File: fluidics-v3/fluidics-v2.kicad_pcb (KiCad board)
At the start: 4 copper layers, 82.5 x 95.5 mm, 77 parts, among them IC2 ADUM1250WSRZ-RL7, J1 PJ-063AH, J10 87832-1010, J11 0705430001, J12 87832-1010, J13 0705430001, J14 87832-1010, J15 0533980671, J16 0705430001, J17 0533980671, J18 87832-1010, J19 0705430001, J2 B6B-ZR-SM4-TF, J20 0533980671, J21 87832-1010, J22 0705430001, J24 0705430001, J25 87832-1010, J3 A-DS_15_A_KG-T4S, J4 B6B-ZR-SM4-TF, J5 Screw_Terminal_01x02, J6 Screw_Terminal_01x02, U1 TPL7407LDR, U11 MAX3221, U12 CD4050BDR, U13 TC7PZ17FU, U2 Teensy4.1, U3 AP7366EA-33W5-7, U4 D24V10FX, U6 LTC4311CSC6-TRPBF

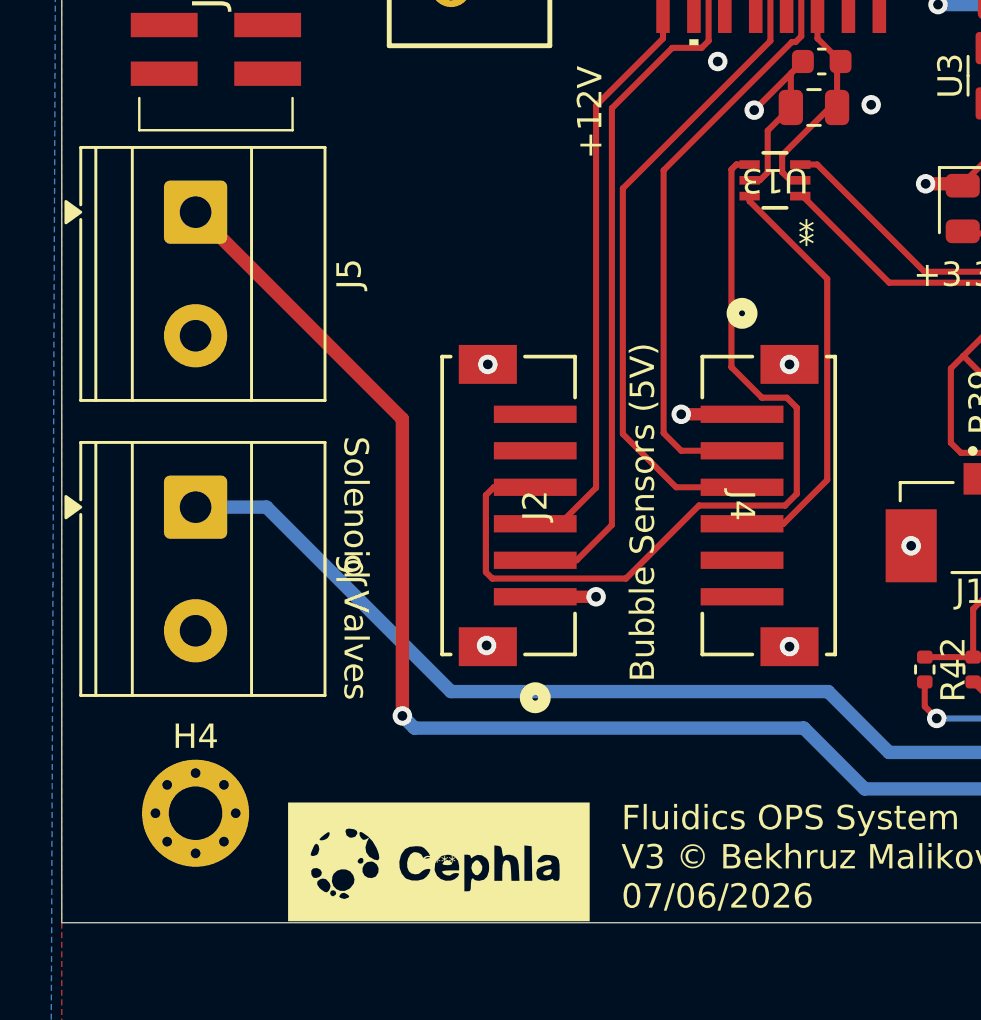
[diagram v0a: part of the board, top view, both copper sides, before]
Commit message: Swap 2x terminal blocks MKDS-1,5-2-5.08 -> MPT-0,5-2-2.54
Replace two 1x02 Phoenix terminal blocks with the smaller MPT series
(2.54mm pitch, 5.54x6.20mm body vs 10.16x9.80mm) to reclaim board space.
Schematic + PCB updated; DRC parity 0. Note: MPT rated for 0.5mm2 wire
(vs 1.5mm2 on MKDS) - lower current/wire-gauge capacity.

Co-Authored-By: Claude Opus 4.8 (1M context) <noreply@anthropic.com>
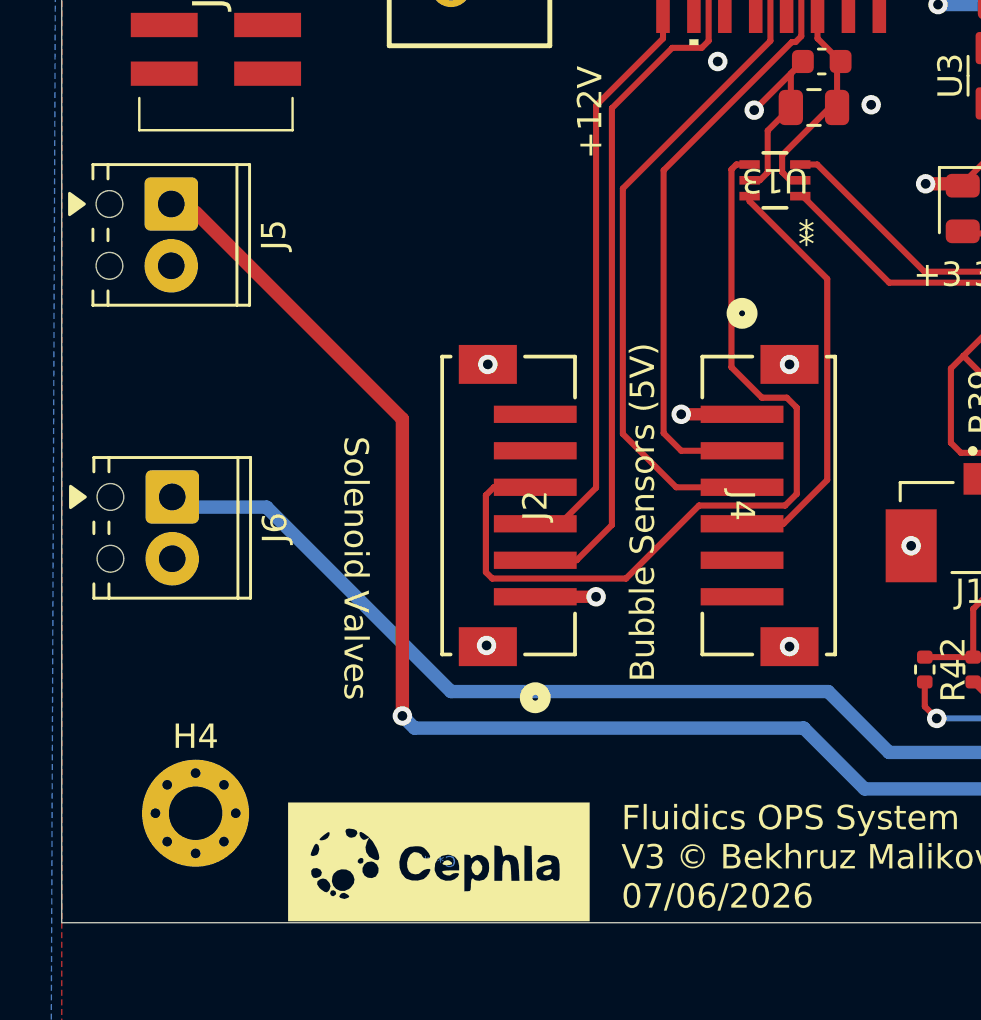
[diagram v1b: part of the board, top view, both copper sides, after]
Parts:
- J5, J6: footprint TerminalBlock_Phoenix:TerminalBlock_Phoenix_MKDS-1,5-2-5.08_1x02_P5.08mm_Horizontal -> TerminalBlock_Phoenix:TerminalBlock_Phoenix_MPT-0,5-2-2.54_1x02_P2.54mm_Horizontal
- moved J5 1.05 mm to (114.0, 87.0)
- moved J6 1.05 mm to (114.0, 99.0)
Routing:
- net Net-(J5-Pin_1): track 109.2 -> 110.4 mm
- net Net-(J6-Pin_1): track 91.1 -> 92.3 mm

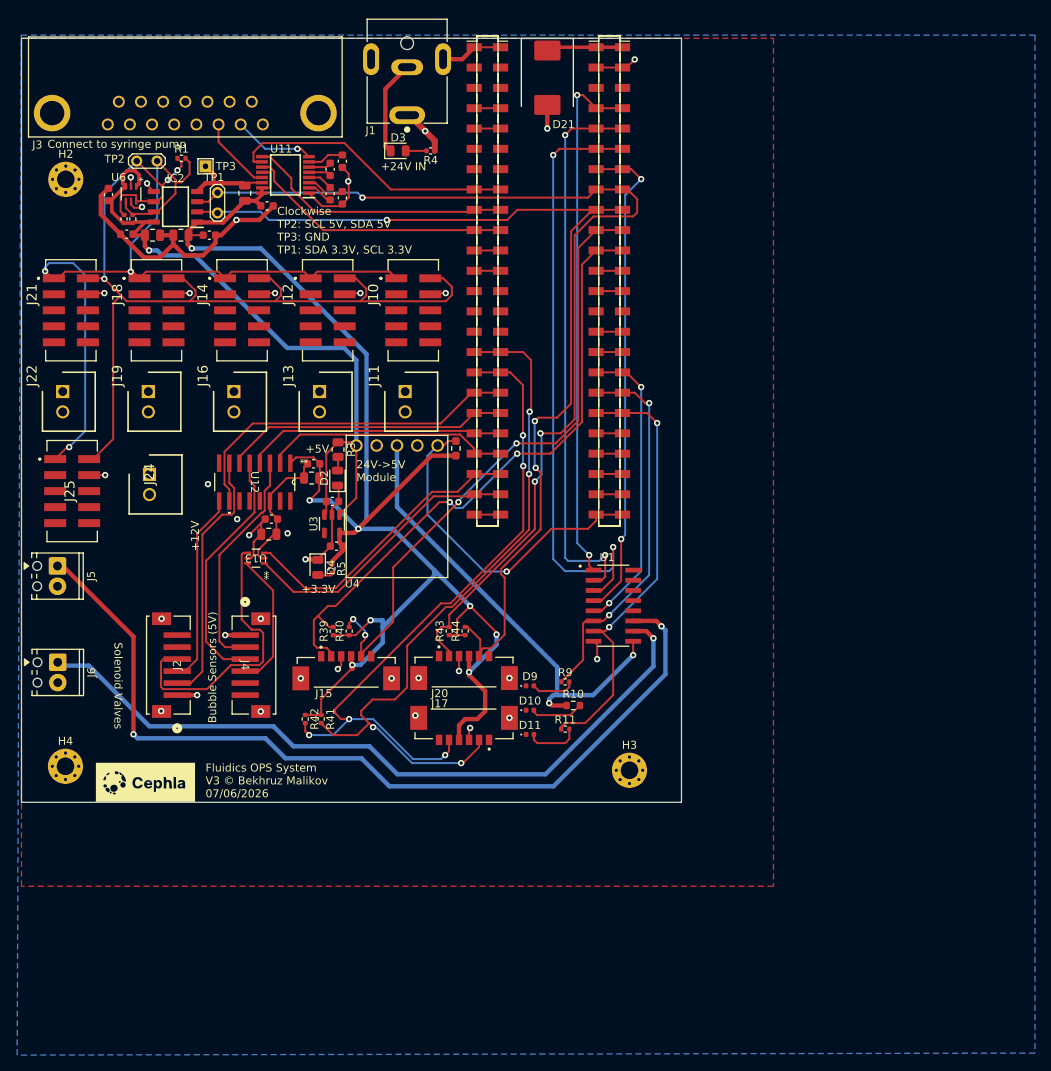
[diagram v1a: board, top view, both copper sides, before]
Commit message: Add GPIO_5 status LED and +24V screw terminal J7
- Root sheet: GPIO_5 status LED (D12 + R12 2.7K to GND)
- Solenoid driver sheet: J7 2-pin screw terminal (pin2 = +24V)

Schematic parses clean via kicad-cli; D12/R12/J7 present in netlist.

Co-Authored-By: Claude Opus 4.8 (1M context) <noreply@anthropic.com>
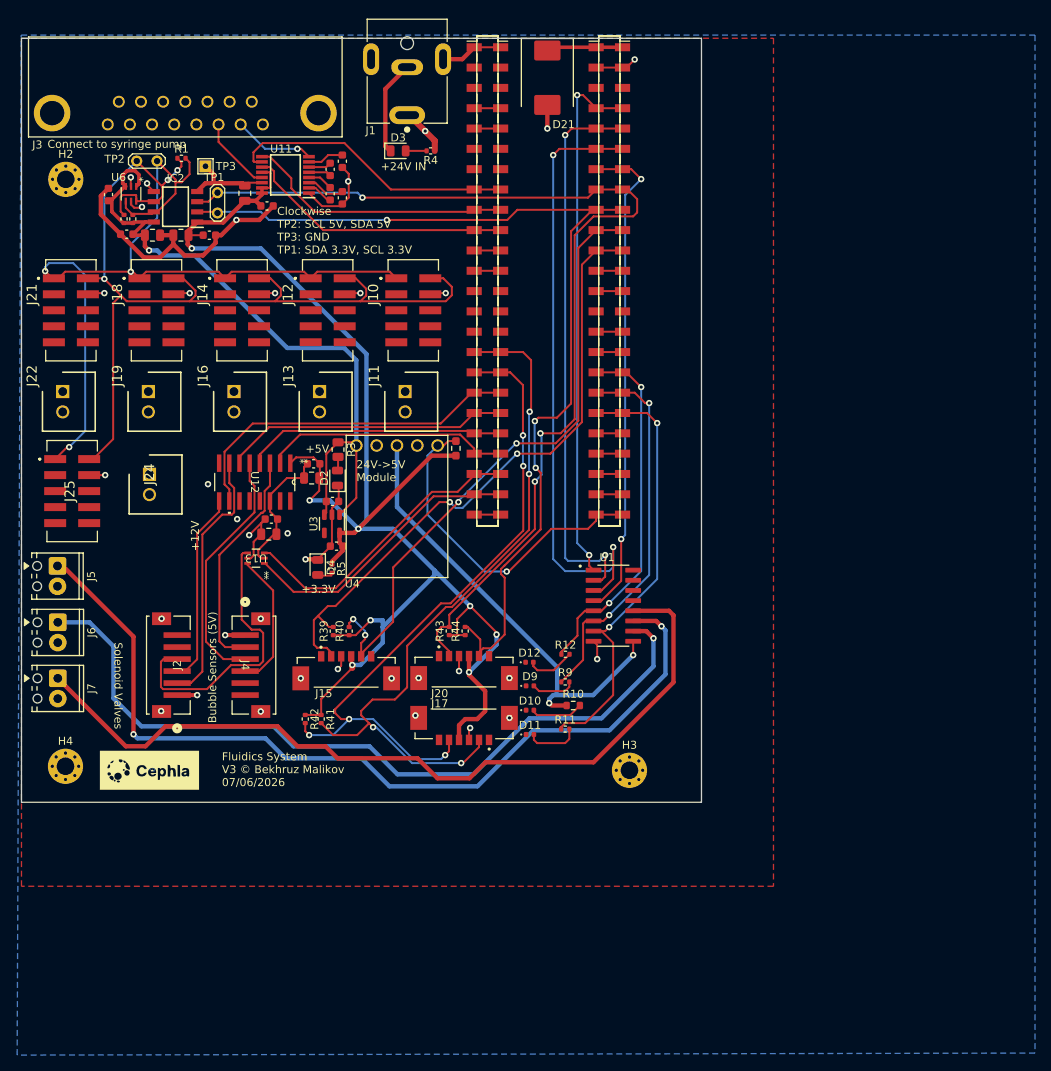
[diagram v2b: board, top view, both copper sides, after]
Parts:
- added D12: LED, LED_SMD:LED_0402_1005Metric, F.Cu at (173.0, 99.0)
- added J7: Screw_Terminal_01x02, TerminalBlock_Phoenix:TerminalBlock_Phoenix_MPT-0,5-2-2.54_1x02_P2.54mm_Horizontal, F.Cu at (114.0, 101.0)
- added R12: 2.7K, Resistor_SMD:R_0402_1005Metric, F.Cu at (177.5, 98.0)
- moved J6 5.00 mm to (114.0, 94.0)
- moved G*** 1.58 mm to (125.5, 112.5)
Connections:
- U1 pad 12: unconnected-(U1-OUT5-Pad12) -> Net-(J7-Pin_1)
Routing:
- net Net-(J7-Pin_1): track 0.00 -> 102.8 mm
- net /GPIO_5: track 37.4 -> 45.1 mm
- net Net-(D12-A): track 0.00 -> 6.05 mm
- net Net-(J6-Pin_1): track 92.3 -> 98.1 mm
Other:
- board size 82.5 x 95.5 mm -> 85 x 95.5 mm
- board text added: "Fluidics System V3 © Bekhruz Malikov 07/06/2026"
- board text removed: "Fluidics OPS System V3 © Bekhruz Malikov 07/06/2026"

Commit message: Consolidate solenoid outputs to single 1x06 terminal J5
Replace 3x 1x02 blocks (J5/J6/J7) with one 6-position Xinya XY308-2.54-6P
(J5): pads 1/3/5 = U1 TPL7407 OUT5/6/7, pads 2/4/6 = +24V. DRC electrically
clean (0 clearance/shorting; 5 unconnected are intentional U2 GPIO/SPI NC).

Assign 3D model: KiCad 10 ships no Xinya XY308 .step, so point J5's model at
the bundled Phoenix MPT-0,5-6-2.54 1x06 (same pitch/positions) for the 3D
preview. Footprint/BOM/CPL still reference the real Xinya part.

Co-Authored-By: Claude Opus 4.8 (1M context) <noreply@anthropic.com>
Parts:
- removed J6, J7: Screw_Terminal_01x02, TerminalBlock_Phoenix:TerminalBlock_Phoenix_MPT-0,5-2-2.54_1x02_P2.54mm_Horizontal
- J5: value Screw_Terminal_01x02 -> Screw_Terminal_01x06; footprint TerminalBlock_Phoenix:TerminalBlock_Phoenix_MPT-0,5-2-2.54_1x02_P2.54mm_Horizontal -> TerminalBlock:TerminalBlock_Xinya_XY308-2.54-6P_1x06_P2.54mm_Horizontal
- moved J5 3.61 mm to (116.0, 90.0)
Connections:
- U1 pad 10: Net-(J6-Pin_1) -> Net-(J5-Pin_5)
- U1 pad 11: Net-(J5-Pin_1) -> Net-(J5-Pin_3)
- U1 pad 12: Net-(J7-Pin_1) -> Net-(J5-Pin_1)
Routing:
- net Net-(J7-Pin_1): track 102.8 -> 0.00 mm
- net Net-(J5-Pin_3): track 0.00 -> 101.1 mm, vias 0 -> 2
- net Net-(J6-Pin_1): track 98.1 -> 0.00 mm, vias 1 -> 0
- net Net-(J5-Pin_5): track 0.00 -> 89.8 mm, vias 0 -> 1
- net Net-(J5-Pin_1): track 110.4 -> 123.3 mm, vias 2 -> 1

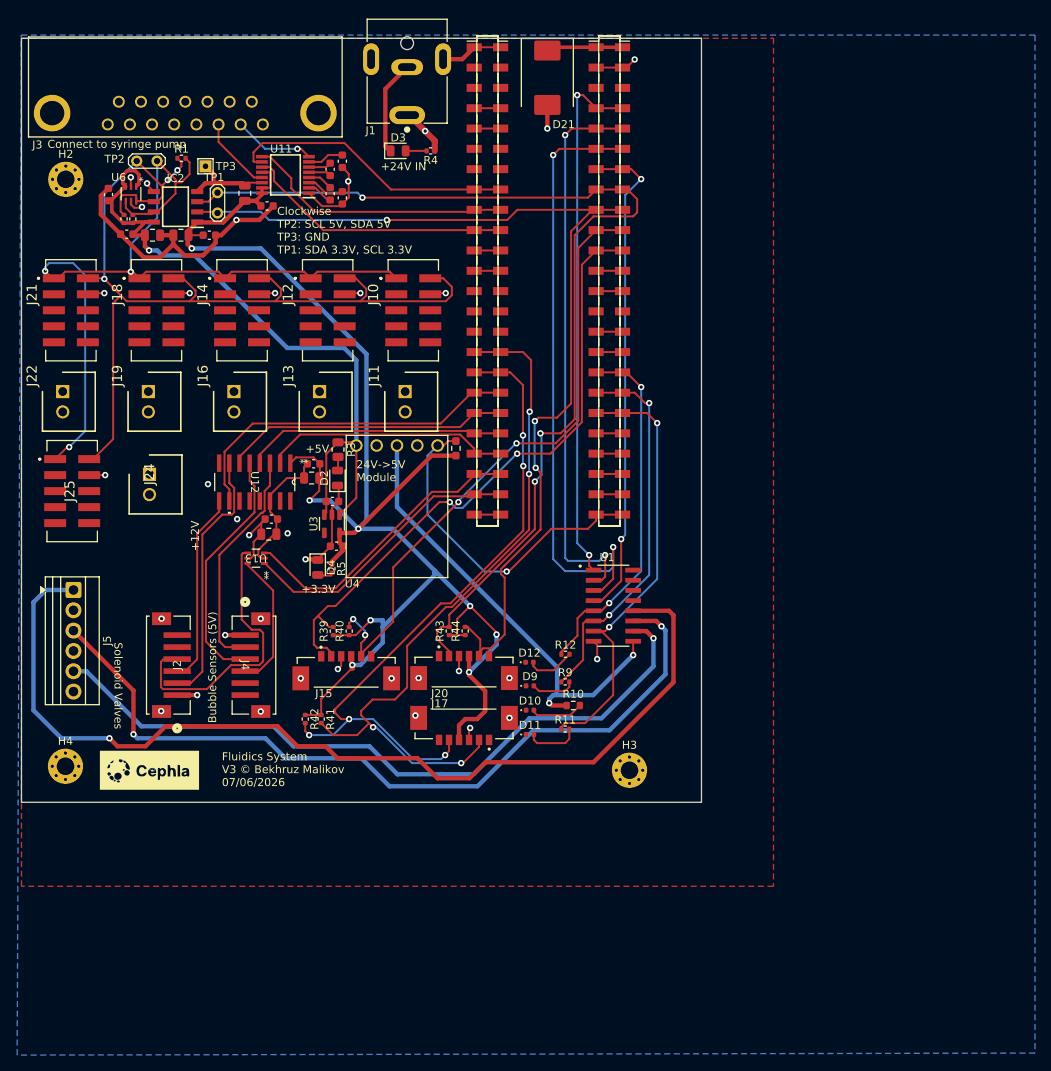
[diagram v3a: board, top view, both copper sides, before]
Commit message: v3 PCB: 3.3V power-plane islands + B.Cu bridge, refdes to F.Fab, block silk labels
PCB (this session, verified DRC-clean, 0 electrical regressions):
- Add +3.3V copper islands on In2.Cu (top U11/IC2 cluster + LDO/I2C-connector corner)
- Add +3.3V bridge pour on B.Cu down the inter-island corridor; delete ~18mm redundant vertical run
- Stitch 3.3V loads to islands with vias; remove ~35mm circuitous surface routing (3.3V trace 194->68mm)
- Move 21 hidden reference designators (caps, R22/R23/R51, U2 Teensy) to F.Fab, centered
- Add functional F.Silkscreen labels: Solenoid Driver, Flow, I2C Iso, RS-232

Also bundles accompanying schematic/library work not authored this session
(fluidics-v2.kicad_sch, svalves, solenoid_driver, 87832-0410 Molex connector lib).

Co-Authored-By: Claude Opus 4.8 (1M context) <noreply@anthropic.com>
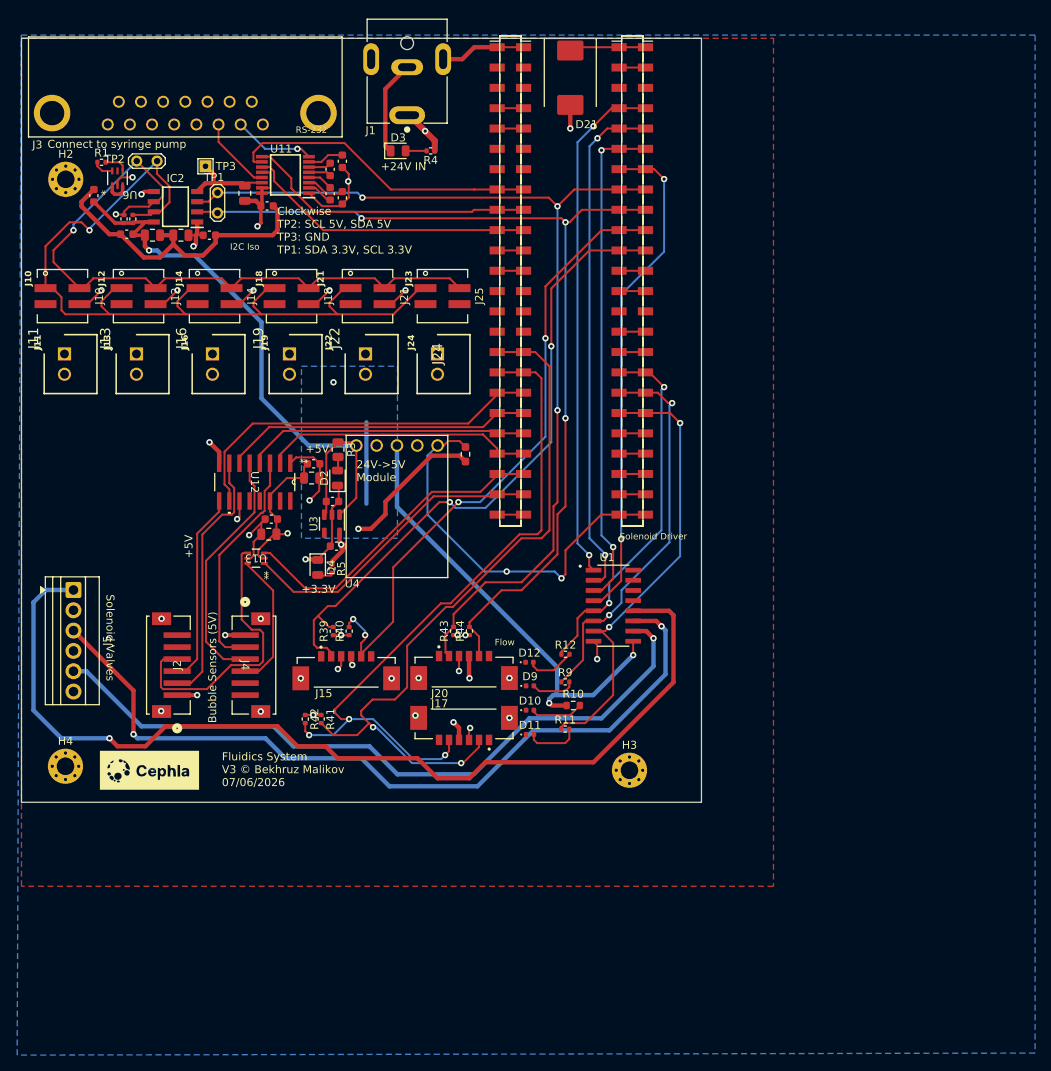
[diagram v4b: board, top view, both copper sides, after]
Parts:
- J10, J12, J14, J18, J21, J25: value 87832-1010 -> 87832-0410; footprint molex_connectors:878321010 -> molex_connectors:878320410
- moved J25 52.3 mm to (162.1, 53.2)
- moved J10 43.9 mm to (114.6, 53.2)
- moved J11 42.8 mm to (114.9, 60.5)
- moved J24 39.0 mm to (161.5, 60.5)
- moved J22 38.1 mm to (152.5, 60.5)
- moved J21 37.1 mm to (152.8, 53.2)
- moved J12 23.7 mm to (124.1, 53.2)
- moved J13 23.4 mm to (123.9, 60.5)
- moved J19 18.3 mm to (143.0, 60.5)
- moved J18 17.0 mm to (143.3, 53.2)
- moved R1 10.0 mm to (119.5, 36.5)
- moved J16 5.41 mm to (133.4, 60.5)
- moved J14 3.87 mm to (133.6, 53.2)
- moved D21 2.87 mm to (178.1, 25.9)
- moved U2 2.87 mm to (178.2, 51.3)
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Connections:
- R1 pad 1: /Selector Valves/SCL 5V -> Net-(U6-BUS1)
- R1 pad 2: /Selector Valves/SDA 5V -> Net-(U6-BUS2)
- U6 pad 4: /Selector Valves/SDA 5V -> Net-(U6-BUS2)
- U6 pad 6: /Selector Valves/SCL 5V -> Net-(U6-BUS1)
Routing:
- net +3.3V: track 194.5 -> 67.6 mm, vias 8 -> 13
- net /Selector Valves/SCL 5V: track 122.1 -> 86.3 mm, vias 3 -> 2
- net +24V: track 62.8 -> 92.5 mm
- net GND: track 133.2 -> 151.7 mm, vias 30 -> 26
- net /GPIO_3: track 77.3 -> 62.8 mm
- net /PG-5V: track 42.4 -> 49.0 mm, vias 1 -> 2
- net /SDA: track 129.2 -> 122.9 mm
- net /GPIO_2: track 70.1 -> 64.2 mm
- net /SCL: track 122.4 -> 118.1 mm
- net +5V: track 102.4 -> 98.1 mm
- net /Bubble Sensors/1B 3.3V: track 32.1 -> 35.7 mm
- net /Bubble Sensors/2B 3.3V: track 43.6 -> 47.0 mm
- net /UART_TX_SYRPUMP: track 33.2 -> 36.4 mm
- net /Bubble Sensors/Calib 1 3.3V: track 35.6 -> 38.8 mm
- net Net-(U6-BUS2): track 0.00 -> 2.99 mm
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- added copper zone on B.Cu, net +3.3V
- added copper zone on In2.Cu, net +3.3V
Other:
- board text added: "Flow"
- board text added: "I2C Iso"
- board text added: "J10"
- board text added: "J11"
- board text added: "J12"
- board text added: "J13"
- board text added: "J14"
- board text added: "J16"
- board text added: "J18"
- board text added: "J19"
- board text added: "J21"
- board text added: "J22"
- board text added: "J23"
- board text added: "J24"
- board text added: "RS-232"
- board text added: "Solenoid Driver"
- board text removed: "+12V"

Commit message: v3 PCB: complete +24V input-protection front-end + downsize bulk caps
Input stage (J1 barrel jack -> TH1 NTC inrush limiter -> +24V plane):
- Fix +24V-into-J1 short + solder-mask bridge (leftover rail track ran
  into the /+24V_IN pad after J1 was repurposed as the input)
- Tie in U6.5 GND and C3 +24V bulk cap; stitch 3 isolated GND pour islands
- Route /+24V_IN on Front at 1.5mm (carries full board +24V current)

Bulk caps downsized, capacitance unchanged, all re-tied via-to-plane:
- C3  100uF/+24V: electrolytic CP_Elec_8x10.5 -> polymer CP_EIA-7343-20 (~2mm)
- C4   47uF/+3V3: electrolytic -> C_1206 ceramic
- C10 100uF/+5V:  electrolytic -> C_1210 ceramic
Schematic footprints updated to match (schematic/PCB parity clean).

DRC: 0 shorts/clearance/hole/isolated/parity; 6 unconnected
(5 intentional U2 no-connects + 1 pre-existing +5V stub gap).

Co-Authored-By: Claude Opus 4.8 (1M context) <noreply@anthropic.com>
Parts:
- added C10: 100u, C_1210_3225Metric, F.Cu at (129.0, 82.5)
- added C3: 100u, CP_EIA-7343-20_Kemet-V, F.Cu at (117.2, 73.5)
- added C4: 47u, C_1206_3216Metric, F.Cu at (156.5, 90.0)
- added TH1: 10R, Varistor:RV_Disc_D7mm_W3.9mm_P5mm, F.Cu at (160.5, 36.0)
- moved D3 1.09 mm to (156.4, 34.0)
- moved R4 1.09 mm to (160.5, 34.0)
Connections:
- J1 pad 1: +24V -> /+24V_IN
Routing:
- net /+24V_IN: track 0.00 -> 15.1 mm
- net +24V: track 92.5 -> 89.5 mm, vias 3 -> 4
- net GND: track 151.7 -> 153.2 mm, vias 26 -> 29
- net +5V: track 98.1 -> 99.1 mm, vias 5 -> 6
- net +3.3V: track 67.6 -> 68.6 mm, vias 13 -> 14
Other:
- board text added: "+24V CAP"
- board text added: "+3.3V CAP"
- board text added: "+5V CAP"
- board text added: "Selector Valves"
